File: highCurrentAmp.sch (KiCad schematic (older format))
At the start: 16 parts, among them U4 AD8021, U5 AD8021

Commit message: Updated all part descriptions
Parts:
- C25, C31: Alt. Order Code (none) -> 77-VJ0603Y103KXACBC; Alt. Supplier (none) -> Mouser; Note (none) -> 10nF/100V X7R 0603 ceramic capacitor; Package (none) -> 0603; Supplier (none) -> Farnell
- C26, C30, C32, C36: Alt. Order Code (none) -> 710-885012206095; Alt. Supplier (none) -> Mouser; Note (none) -> 100nF/50V X7R 0603 ceramic capacitor; Package (none) -> 0603; Supplier (none) -> Farnell
- C27, C29, C33, C35: Alt. Order Code (none) -> 710-885012206081; Alt. Supplier (none) -> Mouser; Note (none) -> 470pF/50V C0G(NP0) 0603 ceramic capacitor; Package (none) -> 0603; Supplier (none) -> Farnell
- C28, C34: Alt. Order Code (none) -> 77-VJ0603A100JXACBC; Alt. Supplier (none) -> Mouser; Manufacturer (none) -> Multicomp; Note (none) -> 10pF/50V C0G(NP0) 0603 ceramic capacitor; Order Code (none) -> 2320799; Package (none) -> 0603; Part Number (none) -> MC0603N100J500CT; Supplier (none) -> Farnell
- R23, R24: Alt. Order Code (none) -> 279-RP73PF2A49R9BTDF; Alt. Supplier (none) -> Mouser; Note (none) -> 49.9Ω/0.1%/250mW 0805 resistor; Package (none) -> 0805; Supplier (none) -> Farnell
- U4, U5: Alt. Order Code (none) -> 584-AD8021ARZ; Alt. Supplier (none) -> Mouser; Note (none) -> Low noise high speed amplifier for 16-bit systems; Package (none) -> SO-8; Supplier (none) -> Farnell
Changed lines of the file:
@@
 EESchema Schematic File Version 2
-LIBS:MicroFLiC_DAC_1_0-rescue
 LIBS:power
 LIBS:device
@@
 LIBS:valves
 LIBS:jakub
-LIBS:MicroFLiC_DAC_1_0-cache
+LIBS:MicroFLiC_DAC-cache
 EELAYER 25 0
 EELAYER END
@@
 F 4 "MC0603N471J500CT" H 3550 2200 60  0001 C CNN "Part Number"
 F 5 "Multicomp" H 3550 2200 60  0001 C CNN "Manufacturer"
-F 6 "1759080" H 3550 2200 60  0001 C CNN "Order Code"
+F 6 "0603" H 3550 2200 60  0001 C CNN "Package"
+F 7 "Farnell" H 3550 2200 60  0001 C CNN "Supplier"
+F 8 "1759080" H 3550 2200 60  0001 C CNN "Order Code"
+F 9 "Mouser" H 3550 2200 60  0001 C CNN "Alt. Supplier"
+F 10 "710-885012206081" H 3550 2200 60  0001 C CNN "Alt. Order Code"
+F 11 "470pF/50V C0G(NP0) 0603 ceramic capacitor" H 3550 2200 60  0001 C CNN "Note"
 	1    3550 2200
 	0    1    1    0
@@
 F 4 "MC0603B104K500CT" H 5300 7000 60  0001 C CNN "Part Number"
 F 5 "Multicomp" H 5300 7000 60  0001 C CNN "Manufacturer"
-F 6 "1759122" H 5300 7000 60  0001 C CNN "Order Code"
+F 6 "0603" H 3550 1900 60  0001 C CNN "Package"
+F 7 "Farnell" H 3550 1900 60  0001 C CNN "Supplier"
+F 8 "1759122" H 5300 7000 60  0001 C CNN "Order Code"
+F 9 "Mouser" H 3550 1900 60  0001 C CNN "Alt. Supplier"
+F 10 "710-885012206095" H 3550 1900 60  0001 C CNN "Alt. Order Code"
+F 11 "100nF/50V X7R 0603 ceramic capacitor" H 3550 1900 60  0001 C CNN "Note"
 	1    3550 1900
 	0    1    1    0
@@
 F 4 "MC0603N471J500CT" H 3550 2200 60  0001 C CNN "Part Number"
 F 5 "Multicomp" H 3550 2200 60  0001 C CNN "Manufacturer"
-F 6 "1759080" H 3550 2200 60  0001 C CNN "Order Code"
+F 6 "0603" H 3600 3350 60  0001 C CNN "Package"
+F 7 "Farnell" H 3600 3350 60  0001 C CNN "Supplier"
+F 8 "1759080" H 3550 2200 60  0001 C CNN "Order Code"
+F 9 "Mouser" H 3600 3350 60  0001 C CNN "Alt. Supplier"
+F 10 "710-885012206081" H 3600 3350 60  0001 C CNN "Alt. Order Code"
+F 11 "470pF/50V C0G(NP0) 0603 ceramic capacitor" H 3600 3350 60  0001 C CNN "Note"
 	1    3600 3350
 	0    1    1    0
@@
 F 4 "MC0603B104K500CT" H 5300 7000 60  0001 C CNN "Part Number"
 F 5 "Multicomp" H 5300 7000 60  0001 C CNN "Manufacturer"
-F 6 "1759122" H 5300 7000 60  0001 C CNN "Order Code"
+F 6 "0603" H 3600 3650 60  0001 C CNN "Package"
+F 7 "Farnell" H 3600 3650 60  0001 C CNN "Supplier"
+F 8 "1759122" H 5300 7000 60  0001 C CNN "Order Code"
+F 9 "Mouser" H 3600 3650 60  0001 C CNN "Alt. Supplier"
+F 10 "710-885012206095" H 3600 3650 60  0001 C CNN "Alt. Order Code"
+F 11 "100nF/50V X7R 0603 ceramic capacitor" H 3600 3650 60  0001 C CNN "Note"
 	1    3600 3650
 	0    1    1    0
@@
 F 4 "MC0603B103K101CT" H 2800 2200 60  0001 C CNN "Part Number"
 F 5 "Multicomp" H 2800 2200 60  0001 C CNN "Manufacturer"
-F 6 "2320786" H 2800 2200 60  0001 C CNN "Order Code"
+F 6 "0603" H 2800 2200 60  0001 C CNN "Package"
+F 7 "Farnell" H 2800 2200 60  0001 C CNN "Supplier"
+F 8 "2320786" H 2800 2200 60  0001 C CNN "Order Code"
+F 9 "Mouser" H 2800 2200 60  0001 C CNN "Alt. Supplier"
+F 10 "77-VJ0603Y103KXACBC" H 2800 2200 60  0001 C CNN "Alt. Order Code"
+F 11 "10nF/100V X7R 0603 ceramic capacitor" H 2800 2200 60  0001 C CNN "Note"
 	1    2800 2200
 	0    1    1    0
@@
 F 4 "MC0603N471J500CT" H 3550 2200 60  0001 C CNN "Part Number"
 F 5 "Multicomp" H 3550 2200 60  0001 C CNN "Manufacturer"
-F 6 "1759080" H 3550 2200 60  0001 C CNN "Order Code"
+F 6 "0603" H 8150 2200 60  0001 C CNN "Package"
+F 7 "Farnell" H 8150 2200 60  0001 C CNN "Supplier"
+F 8 "1759080" H 3550 2200 60  0001 C CNN "Order Code"
+F 9 "Mouser" H 8150 2200 60  0001 C CNN "Alt. Supplier"
+F 10 "710-885012206081" H 8150 2200 60  0001 C CNN "Alt. Order Code"
+F 11 "470pF/50V C0G(NP0) 0603 ceramic capacitor" H 8150 2200 60  0001 C CNN "Note"
 	1    8150 2200
 	0    1    1    0
@@
 F 4 "MC0603B104K500CT" H 5300 7000 60  0001 C CNN "Part Number"
 F 5 "Multicomp" H 5300 7000 60  0001 C CNN "Manufacturer"
-F 6 "1759122" H 5300 7000 60  0001 C CNN "Order Code"
+F 6 "0603" H 8150 1900 60  0001 C CNN "Package"
+F 7 "Farnell" H 8150 1900 60  0001 C CNN "Supplier"
+F 8 "1759122" H 5300 7000 60  0001 C CNN "Order Code"
+F 9 "Mouser" H 8150 1900 60  0001 C CNN "Alt. Supplier"
+F 10 "710-885012206095" H 8150 1900 60  0001 C CNN "Alt. Order Code"
+F 11 "100nF/50V X7R 0603 ceramic capacitor" H 8150 1900 60  0001 C CNN "Note"
 	1    8150 1900
 	0    1    1    0
@@
 F 4 "MC0603N471J500CT" H 3550 2200 60  0001 C CNN "Part Number"
 F 5 "Multicomp" H 3550 2200 60  0001 C CNN "Manufacturer"
-F 6 "1759080" H 3550 2200 60  0001 C CNN "Order Code"
+F 6 "0603" H 8200 3350 60  0001 C CNN "Package"
+F 7 "Farnell" H 8200 3350 60  0001 C CNN "Supplier"
+F 8 "1759080" H 3550 2200 60  0001 C CNN "Order Code"
+F 9 "Mouser" H 8200 3350 60  0001 C CNN "Alt. Supplier"
+F 10 "710-885012206081" H 8200 3350 60  0001 C CNN "Alt. Order Code"
+F 11 "470pF/50V C0G(NP0) 0603 ceramic capacitor" H 8200 3350 60  0001 C CNN "Note"
 	1    8200 3350
 	0    1    1    0
@@
 F 4 "MC0603B104K500CT" H 5300 7000 60  0001 C CNN "Part Number"
 F 5 "Multicomp" H 5300 7000 60  0001 C CNN "Manufacturer"
-F 6 "1759122" H 5300 7000 60  0001 C CNN "Order Code"
+F 6 "0603" H 8200 3650 60  0001 C CNN "Package"
+F 7 "Farnell" H 8200 3650 60  0001 C CNN "Supplier"
+F 8 "1759122" H 5300 7000 60  0001 C CNN "Order Code"
+F 9 "Mouser" H 8200 3650 60  0001 C CNN "Alt. Supplier"
+F 10 "710-885012206095" H 8200 3650 60  0001 C CNN "Alt. Order Code"
+F 11 "100nF/50V X7R 0603 ceramic capacitor" H 8200 3650 60  0001 C CNN "Note"
 	1    8200 3650
 	0    1    1    0
@@
 F 4 "MC0603B103K101CT" H 7400 2200 60  0001 C CNN "Part Number"
 F 5 "Multicomp" H 7400 2200 60  0001 C CNN "Manufacturer"
-F 6 "2320786" H 7400 2200 60  0001 C CNN "Order Code"
+F 6 "0603" H 7400 2200 60  0001 C CNN "Package"
+F 7 "Farnell" H 7400 2200 60  0001 C CNN "Supplier"
+F 8 "2320786" H 7400 2200 60  0001 C CNN "Order Code"
+F 9 "Mouser" H 7400 2200 60  0001 C CNN "Alt. Supplier"
+F 10 "77-VJ0603Y103KXACBC" H 7400 2200 60  0001 C CNN "Alt. Order Code"
+F 11 "10nF/100V X7R 0603 ceramic capacitor" H 7400 2200 60  0001 C CNN "Note"
 	1    7400 2200
 	0    1    1    0
@@
 F 4 "AD8021ARZ" H 3300 2700 60  0001 C CNN "Part Number"
 F 5 "Analog Devices" H 3300 2700 60  0001 C CNN "Manufacturer"
-F 6 "9426000" H 3300 2700 60  0001 C CNN "Order Code"
+F 6 "SO-8" H 3300 2700 60  0001 C CNN "Package"
+F 7 "Farnell" H 3300 2700 60  0001 C CNN "Supplier"
+F 8 "9426000" H 3300 2700 60  0001 C CNN "Order Code"
+F 9 "Mouser" H 3300 2700 60  0001 C CNN "Alt. Supplier"
+F 10 "584-AD8021ARZ" H 3300 2700 60  0001 C CNN "Alt. Order Code"
+F 11 "Low noise high speed amplifier for 16-bit systems" H 3300 2700 60  0001 C CNN "Note"
 	1    3300 2700
 	1    0    0    -1
@@
 F 2 "Capacitors_SMD:C_0603" H 3638 2900 30  0001 C CNN
 F 3 "" H 3600 3050 60  0000 C CNN
+F 4 "MC0603N100J500CT" H 3600 3050 60  0001 C CNN "Part Number"
+F 5 "Multicomp" H 3600 3050 60  0001 C CNN "Manufacturer"
+F 6 "0603" H 3600 3050 60  0001 C CNN "Package"
+F 7 "Farnell" H 3600 3050 60  0001 C CNN "Supplier"
+F 8 "2320799" H 3600 3050 60  0001 C CNN "Order Code"
+F 9 "Mouser" H 3600 3050 60  0001 C CNN "Alt. Supplier"
+F 10 "77-VJ0603A100JXACBC" H 3600 3050 60  0001 C CNN "Alt. Order Code"
+F 11 "10pF/50V C0G(NP0) 0603 ceramic capacitor" H 3600 3050 60  0001 C CNN "Note"
 	1    3600 3050
 	0    1    1    0
@@
 F 4 "AD8021ARZ" H 7900 2700 60  0001 C CNN "Part Number"
 F 5 "Analog Devices" H 7900 2700 60  0001 C CNN "Manufacturer"
-F 6 "9426000" H 7900 2700 60  0001 C CNN "Order Code"
+F 6 "SO-8" H 7900 2700 60  0001 C CNN "Package"
+F 7 "Farnell" H 7900 2700 60  0001 C CNN "Supplier"
+F 8 "9426000" H 7900 2700 60  0001 C CNN "Order Code"
+F 9 "Mouser" H 7900 2700 60  0001 C CNN "Alt. Supplier"
+F 10 "584-AD8021ARZ" H 7900 2700 60  0001 C CNN "Alt. Order Code"
+F 11 "Low noise high speed amplifier for 16-bit systems" H 7900 2700 60  0001 C CNN "Note"
 	1    7900 2700
 	1    0    0    -1
@@
 F 2 "Capacitors_SMD:C_0603" H 8238 2900 30  0001 C CNN
 F 3 "" H 8200 3050 60  0000 C CNN
+F 4 "MC0603N100J500CT" H 8200 3050 60  0001 C CNN "Part Number"
+F 5 "Multicomp" H 8200 3050 60  0001 C CNN "Manufacturer"
+F 6 "0603" H 8200 3050 60  0001 C CNN "Package"
+F 7 "Farnell" H 8200 3050 60  0001 C CNN "Supplier"
+F 8 "2320799" H 8200 3050 60  0001 C CNN "Order Code"
+F 9 "Mouser" H 8200 3050 60  0001 C CNN "Alt. Supplier"
+F 10 "77-VJ0603A100JXACBC" H 8200 3050 60  0001 C CNN "Alt. Order Code"
+F 11 "10pF/50V C0G(NP0) 0603 ceramic capacitor" H 8200 3050 60  0001 C CNN "Note"
 	1    8200 3050
 	0    1    1    0
@@
 F 4 "RP73PF2A49R9BTDF" V 4450 2700 60  0001 C CNN "Part Number"
 F 5 "TE Connectivity" V 4450 2700 60  0001 C CNN "Manufacturer"
-F 6 "2117023" V 4450 2700 60  0001 C CNN "Order Code"
+F 6 "0805" H 4450 2700 60  0001 C CNN "Package"
+F 7 "Farnell" H 4450 2700 60  0001 C CNN "Supplier"
+F 8 "2117023" V 4450 2700 60  0001 C CNN "Order Code"
+F 9 "Mouser" H 4450 2700 60  0001 C CNN "Alt. Supplier"
+F 10 "279-RP73PF2A49R9BTDF" H 4450 2700 60  0001 C CNN "Alt. Order Code"
+F 11 "49.9Ω/0.1%/250mW 0805 resistor" H 4450 2700 60  0001 C CNN "Note"
 	1    4450 2700
 	0    1    1    0
@@
 F 4 "RP73PF2A49R9BTDF" V 9050 2700 60  0001 C CNN "Part Number"
 F 5 "TE Connectivity" V 9050 2700 60  0001 C CNN "Manufacturer"
-F 6 "2117023" V 9050 2700 60  0001 C CNN "Order Code"
+F 6 "0805" H 9050 2700 60  0001 C CNN "Package"
+F 7 "Farnell" H 9050 2700 60  0001 C CNN "Supplier"
+F 8 "2117023" V 9050 2700 60  0001 C CNN "Order Code"
+F 9 "Mouser" H 9050 2700 60  0001 C CNN "Alt. Supplier"
+F 10 "279-RP73PF2A49R9BTDF" H 9050 2700 60  0001 C CNN "Alt. Order Code"
+F 11 "49.9Ω/0.1%/250mW 0805 resistor" H 9050 2700 60  0001 C CNN "Note"
 	1    9050 2700
 	0    1    1    0

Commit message: Fixed SO-8 to SOIC-8
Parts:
- U4, U5: Package SO-8 -> SOIC-8
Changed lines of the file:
@@
 F 4 "AD8021ARZ" H 3300 2700 60  0001 C CNN "Part Number"
 F 5 "Analog Devices" H 3300 2700 60  0001 C CNN "Manufacturer"
-F 6 "SO-8" H 3300 2700 60  0001 C CNN "Package"
+F 6 "SOIC-8" H 3300 2700 60  0001 C CNN "Package"
 F 7 "Farnell" H 3300 2700 60  0001 C CNN "Supplier"
 F 8 "9426000" H 3300 2700 60  0001 C CNN "Order Code"
@@
 F 4 "AD8021ARZ" H 7900 2700 60  0001 C CNN "Part Number"
 F 5 "Analog Devices" H 7900 2700 60  0001 C CNN "Manufacturer"
-F 6 "SO-8" H 7900 2700 60  0001 C CNN "Package"
+F 6 "SOIC-8" H 7900 2700 60  0001 C CNN "Package"
 F 7 "Farnell" H 7900 2700 60  0001 C CNN "Supplier"
 F 8 "9426000" H 7900 2700 60  0001 C CNN "Order Code"

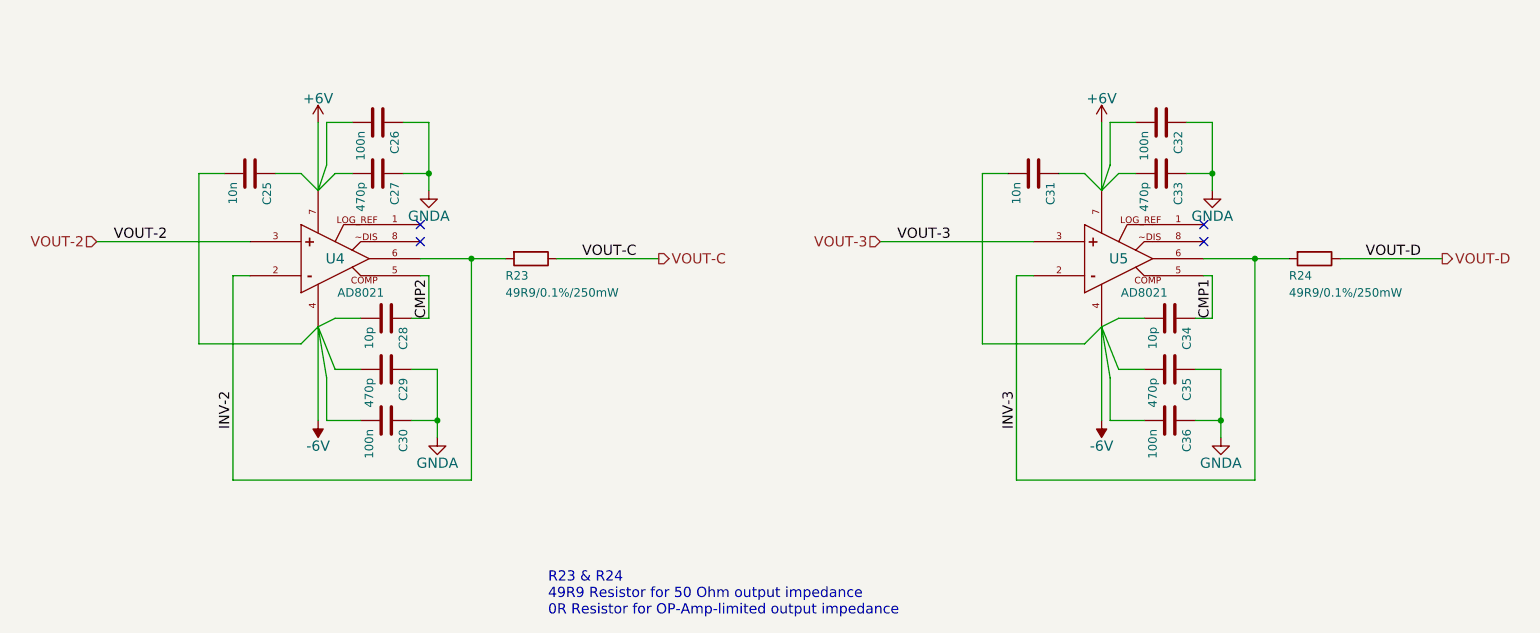
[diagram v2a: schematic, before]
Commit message: Fixed ground problems, added bypass capacitors, added resistor between digital isolator and DAC
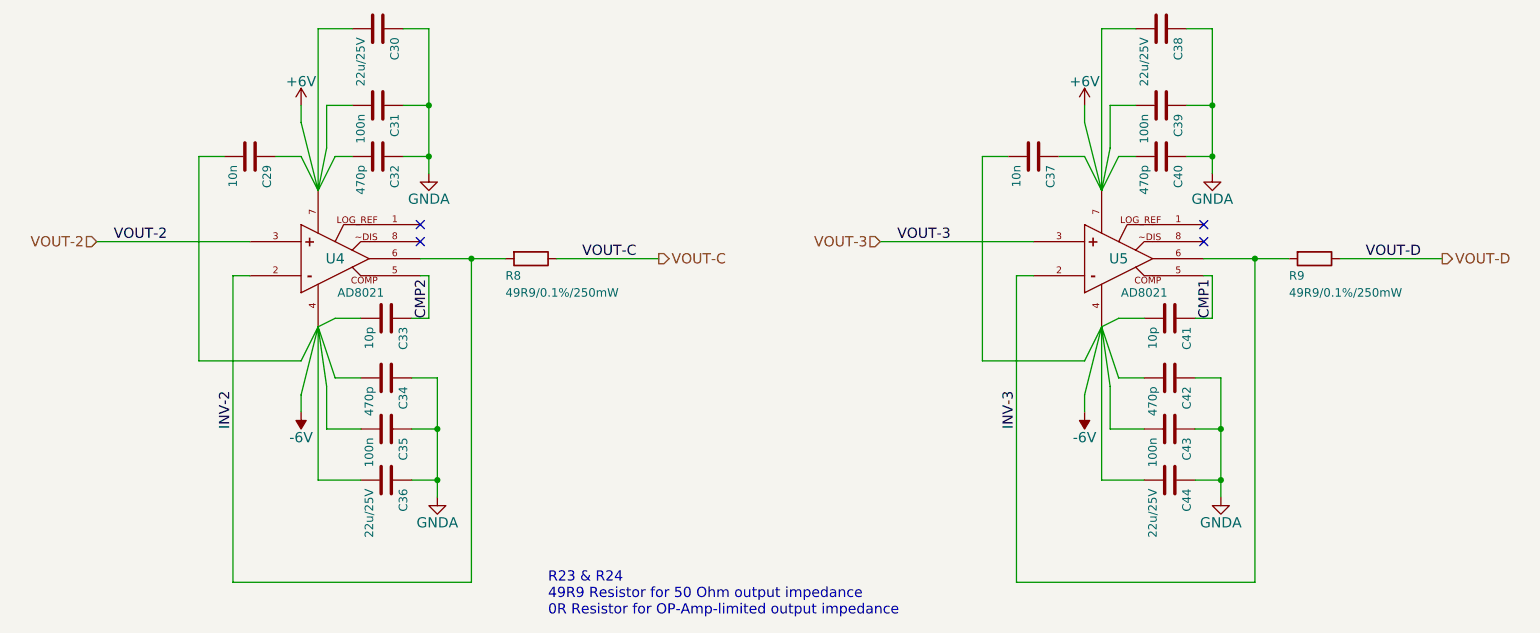
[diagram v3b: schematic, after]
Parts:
- added C30, C36, C38, C44: 22u/25V, Capacitors_SMD:C_1210, symbol C
- renumbered C25 to C29, C26 to C31, C27 to C32, C28 to C33, C29 to C34, C30 to C35, C31 to C37, C32 to C39, C33 to C40, C34 to C41, C35 to C42, C36 to C43, R23 to R8, R24 to R9
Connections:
- net +6V: now also C30.2, C38.2
- net -6V: now also C36.2, C44.2
- net GNDA: now also C30.1, C36.1, C38.1, C44.1
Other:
- moved on the sheet: C29, C31, C32, C34, C35, C37, C39, C40, C42, C43
